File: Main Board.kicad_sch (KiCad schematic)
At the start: 114 parts, among them J102 Speaker Out, J110 SD Holder MEM2061-01-188-00-A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, J2 I2C_MAIN, J3 I2C_A, J4 I2C_B, J45 VCC Select, J49 NEOPIXEL AUX, J85 I2C_C, J86 I2C_D, J87 I2C_E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

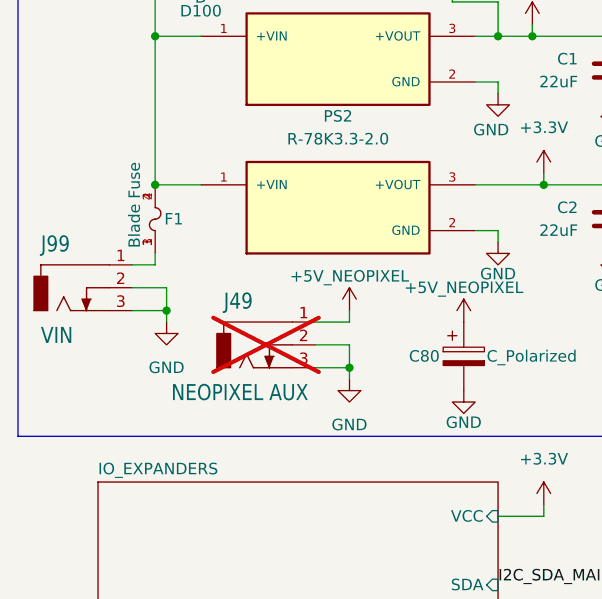
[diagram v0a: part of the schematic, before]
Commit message: Refining BOM & X4
X4 included a diode to protect from reverse polarity DC input. Begun work on Digikey BOM
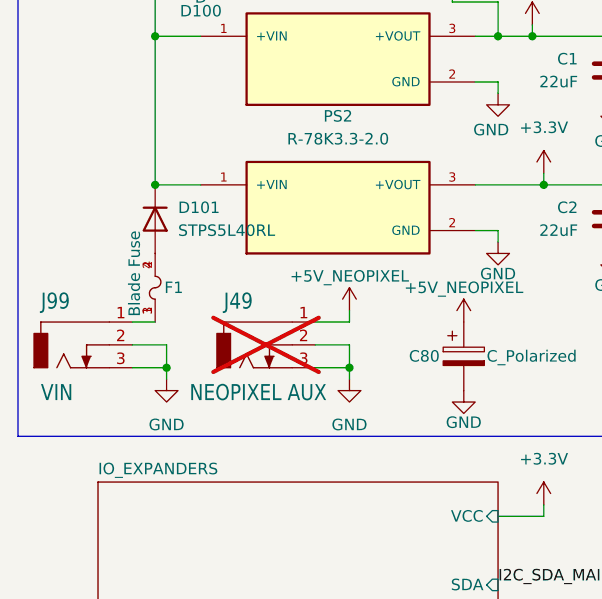
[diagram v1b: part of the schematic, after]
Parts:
- added D101: STPS5L40RL, Diode_THT:D_DO-201AD_P15.24mm_Horizontal, symbol Diode:1N5400
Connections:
- net +12V: now also D101.1 (K); no longer F1.2, F1.4
- new net: D101.2 (A), F1.2, F1.4
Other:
- moved on the sheet: F1, J99
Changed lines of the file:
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@@
 		(title "Main Universal Panel Board")
 		(date "2025-08-06")
-		(rev "X2")
+		(rev "X4")
 		(company "CMSC")
 		(comment 1 "NF 2025")
@@
 	)
 	(junction
-		(at 27.94 128.27)
-		(diameter 0)
-		(color 0 0 0 0)
-	)
-	(junction
 		(at 207.01 223.52)
 		(diameter 0)
@@
 	)
 	(junction
+		(at 27.94 128.27)
+		(diameter 0)
+		(color 0 0 0 0)
+	)
+	(junction
 		(at 358.14 77.47)
 		(diameter 0)
@@
 	)
 	(junction
-		(at 29.21 142.24)
+		(at 29.21 148.59)
 		(diameter 0)
 		(color 0 0 0 0)
@@
 	(wire
 		(pts
-			(xy 27.94 135.89) (xy 27.94 137.16)
-		)
-		(stroke
-			(width 0)
-			(type default)
-		)
-	)
-	(wire
-		(pts
 			(xy 39.37 57.15) (xy 39.37 59.69)
 		)
@@
 	(wire
 		(pts
-			(xy 29.21 142.24) (xy 29.21 143.51)
+			(xy 29.21 148.59) (xy 29.21 149.86)
 		)
 		(stroke
@@
 	(wire
 		(pts
-			(xy 27.94 137.16) (xy 25.4 137.16)
+			(xy 27.94 143.51) (xy 25.4 143.51)
 		)
 		(stroke
@@
 	(wire
 		(pts
-			(xy 29.21 139.7) (xy 29.21 142.24)
+			(xy 29.21 146.05) (xy 29.21 148.59)
 		)
 		(stroke
@@
 	(wire
 		(pts
-			(xy 25.4 139.7) (xy 29.21 139.7)
+			(xy 25.4 146.05) (xy 29.21 146.05)
 		)
 		(stroke
@@
 	(wire
 		(pts
-			(xy 25.4 142.24) (xy 29.21 142.24)
+			(xy 25.4 148.59) (xy 29.21 148.59)
 		)
 		(stroke
@@
 	)
 	(symbol
+		(lib_id "Diode:1N5400")
+		(at 27.94 132.08 270)
+		(unit 1)
+		(exclude_from_sim no)
+		(in_bom yes)
+		(on_board yes)
+		(dnp no)
+		(fields_autoplaced yes)
+		(property "Reference" "D101"
+			(at 30.48 130.8099 90)
+			(effects
+				(font
+					(size 1.27 1.27)
+				)
+				(justify left)
+			)
+		)
+		(property "Value" "STPS5L40RL"
+			(at 30.48 133.3499 90)
+			(effects
+				(font
+					(size 1.27 1.27)
+				)
+				(justify left)
+			)
+		)
+		(property "Footprint" "Diode_THT:D_DO-201AD_P15.24mm_Horizontal"
+			(at 23.495 132.08 0)
+			(effects
+				(font
+					(size 1.27 1.27)
+				)
+				(hide yes)
+			)
+		)
+		(property "Datasheet" "https://www.st.com/content/ccc/resource/technical/document/datasheet/18/17/66/c2/80/47/46/08/CD00002923.pdf/files/CD00002923.pdf/jcr:content/translations/en.CD00002923.pdf"
+			(at 27.94 132.08 0)
+			(effects
+				(font
+					(size 1.27 1.27)
+				)
+				(hide yes)
+			)
+		)
+		(property "Description" "Diode 40 V 5A Through Hole DO-201AD"
+			(at 27.94 132.08 0)
+			(effects
+				(font
+					(size 1.27 1.27)
+				)
+				(hide yes)
+			)
+		)
+		(property "Sim.Device" "D"
+			(at 27.94 132.08 0)
+			(effects
+				(font
+					(size 1.27 1.27)
+				)
+				(hide yes)
+			)
+		)
+		(property "Sim.Pins" "1=K 2=A"
+			(at 27.94 132.08 0)
+			(effects
+				(font
+					(size 1.27 1.27)
+				)
+				(hide yes)
+			)
+		)
+		(pin "2"
+		)
+		(pin "1"
+		)
+		(instances
+			(project ""
+				(path "/2aa9f2df-d06f-4a30-97ab-fb4628a40b5a"
+					(reference "D101")
+					(unit 1)
+				)
+			)
+		)
+	)
+	(symbol
 		(lib_id "power:+3.3V")
 		(at 120.65 144.78 0)
@@
 	(symbol
 		(lib_id "power:GND")
-		(at 29.21 143.51 0)
+		(at 29.21 149.86 0)
 		(mirror y)
 		(unit 1)
@@
 		(fields_autoplaced yes)
 		(property "Reference" "#PWR074"
-			(at 29.21 149.86 0)
+			(at 29.21 156.21 0)
 			(effects
 				(font
@@
 		)
 		(property "Value" "GND"
-			(at 29.21 148.59 0)
+			(at 29.21 154.94 0)
 			(effects
 				(font
@@
 		)
 		(property "Footprint" ""
-			(at 29.21 143.51 0)
+			(at 29.21 149.86 0)
 			(effects
 				(font
@@
 		)
 		(property "Datasheet" ""
-			(at 29.21 143.51 0)
+			(at 29.21 149.86 0)
 			(effects
 				(font
@@
 		)
 		(property "Description" "Power symbol creates a global label with name \"GND\" , ground"
-			(at 29.21 143.51 0)
+			(at 29.21 149.86 0)
 			(effects
 				(font
@@
 	(symbol
 		(lib_id "New_Panel_Parts:Blade Fuse Holder 3568")
-		(at 27.94 132.08 90)
+		(at 27.94 139.7 90)
 		(unit 1)
 		(exclude_from_sim no)
@@
 		(dnp no)
 		(property "Reference" "F1"
-			(at 28.956 132.08 90)
+			(at 28.956 139.7 90)
 			(effects
 				(font
@@
 		)
 		(property "Value" "Blade Fuse"
-			(at 25.654 125.73 0)
+			(at 25.654 133.35 0)
 			(effects
 				(font
@@
 		)
 		(property "Footprint" "New Panel Parts:FUSE_3568"
-			(at 18.034 131.826 0)
+			(at 18.034 139.446 0)
 			(effects
 				(font
@@
 		)
 		(property "Datasheet" ""
-			(at 27.94 132.08 0)
+			(at 27.94 139.7 0)
 			(effects
 				(font
@@
 		)
 		(property "Description" ""
-			(at 27.94 132.08 0)
+			(at 27.94 139.7 0)
 			(effects
 				(font
@@
 		)
 		(property "PARTREV" "C"
-			(at 18.034 131.826 0)
+			(at 18.034 139.446 0)
 			(effects
 				(font
@@
 		)
 		(property "MANUFACTURER" "Keystone"
-			(at 18.034 131.826 0)
+			(at 18.034 139.446 0)
 			(effects
 				(font
@@
 		)
 		(property "SNAPEDA_PN" "3568"
-			(at 18.034 131.826 0)
+			(at 18.034 139.446 0)
 			(effects
 				(font
@@
 		)
 		(property "MAXIMUM_PACKAGE_HEIGHT" "7.37 mm"
-			(at 18.034 131.826 0)
+			(at 18.034 139.446 0)
 			(effects
 				(font
@@
 		)
 		(property "STANDARD" "Manufacturer Recommendations"
-			(at 18.034 131.826 0)
+			(at 18.034 139.446 0)
 			(effects
 				(font
@@
 	(symbol
 		(lib_id "main-eagle-import:DCJ0303")
-		(at 17.78 139.7 0)
+		(at 17.78 146.05 0)
 		(unit 1)
 		(exclude_from_sim no)
@@
 		(dnp no)
 		(property "Reference" "J99"
-			(at 15.24 135.89 0)
+			(at 15.24 142.24 0)
 			(effects
 				(font
@@
 		)
 		(property "Value" "VIN"
-			(at 15.24 146.05 0)
+			(at 15.24 152.4 0)
 			(effects
 				(font
@@
 		)
 		(property "Footprint" "Connector_BarrelJack:BarrelJack_Horizontal"
-			(at 17.78 139.7 0)
+			(at 17.78 146.05 0)
 			(effects
 				(font
@@
 		)
 		(property "Datasheet" ""
-			(at 17.78 139.7 0)
+			(at 17.78 146.05 0)
 			(effects
 				(font
@@
 		)
 		(property "Description" ""
-			(at 17.78 139.7 0)
+			(at 17.78 146.05 0)
 			(effects
 				(font
@@
 		)
 		(property "Value" "NEOPIXEL AUX"
-			(at 29.718 152.4 0)
+			(at 31.75 152.4 0)
 			(effects
 				(font

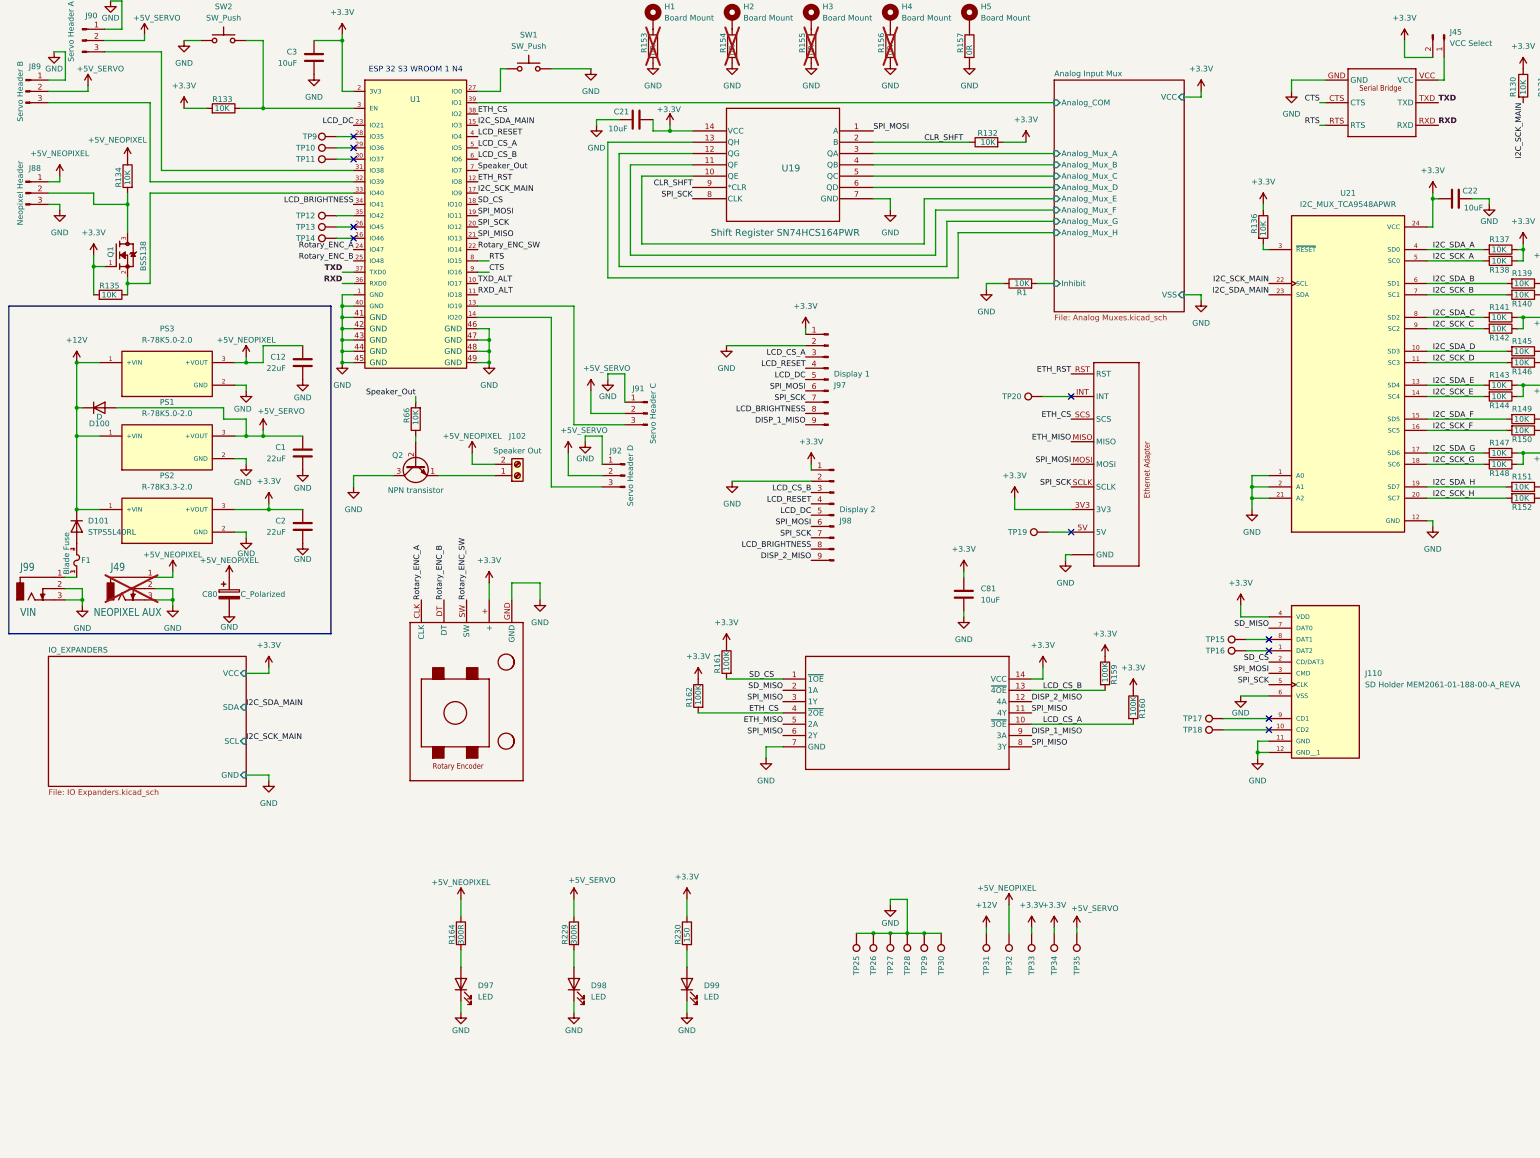
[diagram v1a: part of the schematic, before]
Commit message: Rev A0
REV A0 changes, additionally added STEP files for PAM8302, MAX98357, and JST XH 4 connector for UART. Updated KiCad schematic and PCB files, reorganized BOM and pick-and-place files for new revisions, and refreshed CAM data.
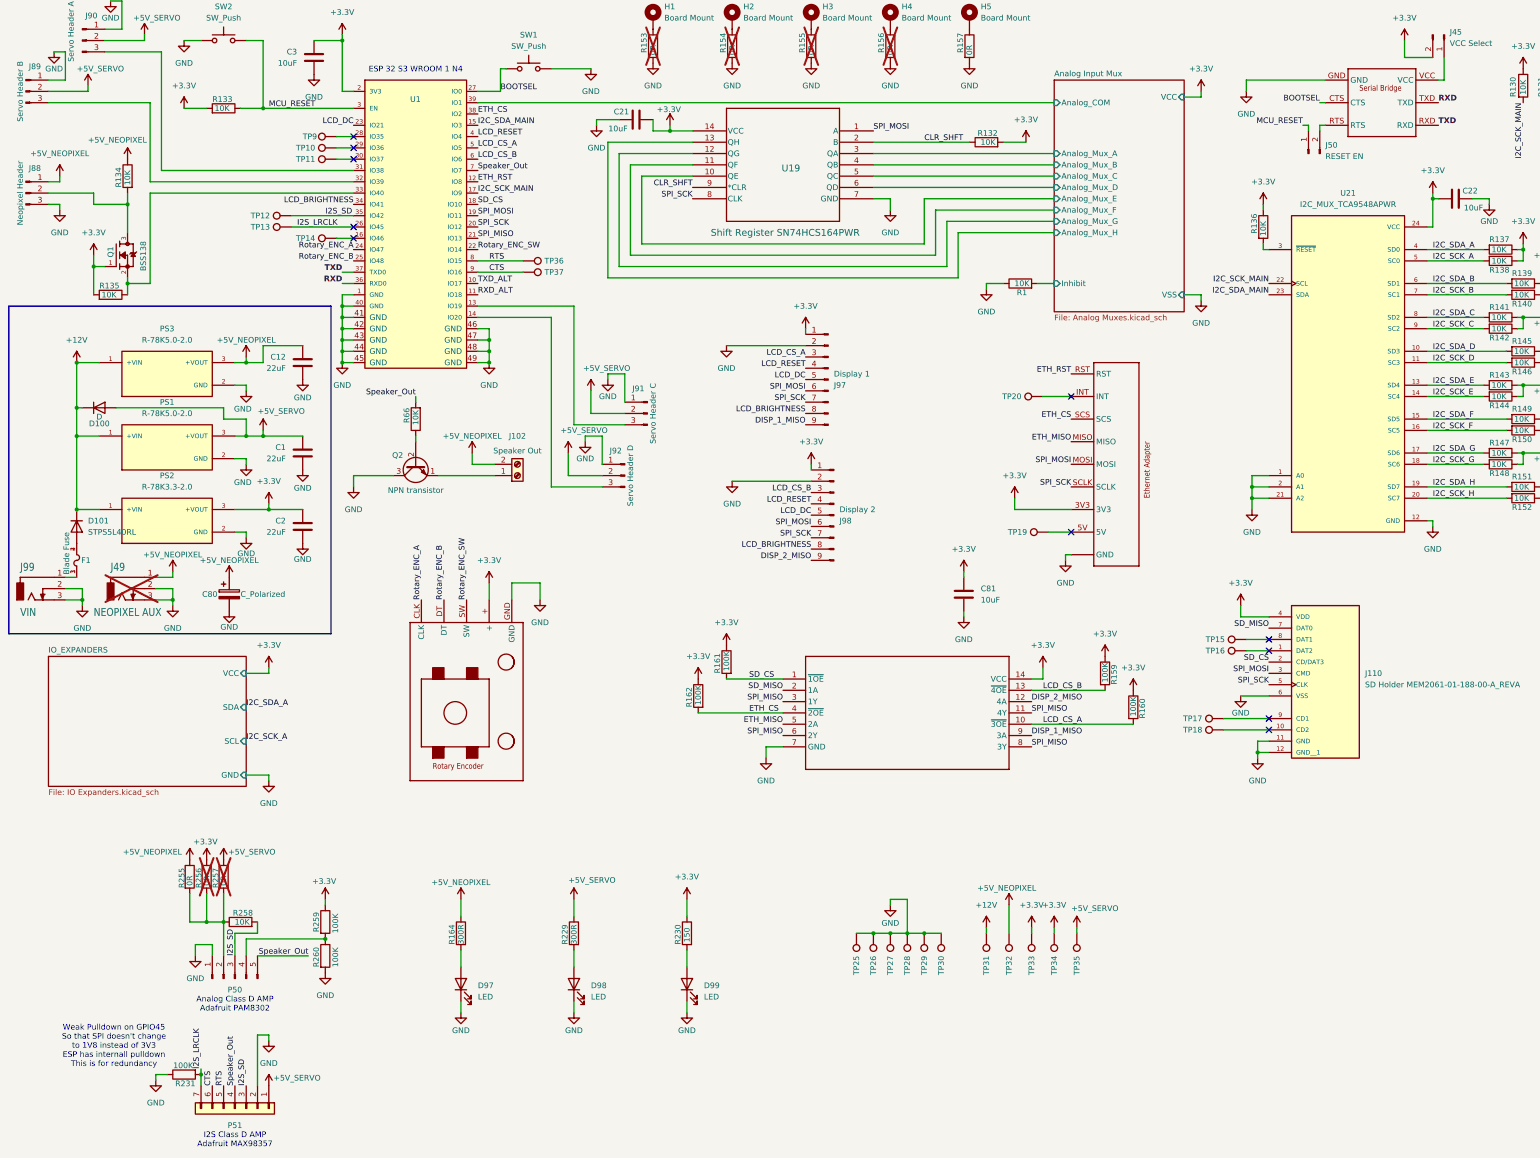
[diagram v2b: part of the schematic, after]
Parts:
- added J50: RESET EN, Connector_PinHeader_2.54mm:PinHeader_1x02_P2.54mm_Vertical, symbol Connector:Conn_01x02_Pin
- added P50: Conn_01x05_Pin, Connector_PinHeader_2.54mm:PinHeader_1x05_P2.54mm_Vertical, symbol Connector:Conn_01x05_Pin
- added P51: Conn_01x07, Connector_PinHeader_2.54mm:PinHeader_1x07_P2.54mm_Vertical, symbol Connector_Generic:Conn_01x07
- added R231, R259, R260: 100K, Resistor_SMD:R_0603_1608Metric, symbol Device:R
- added R255, R256, R257: 0R, Resistor_SMD:R_0603_1608Metric, symbol Device:R
- added R258: 10K, Resistor_SMD:R_0603_1608Metric, symbol Device:R
- added TP36, TP37: TestPoint, Connector_Pin:Pin_D1.0mm_L10.0mm, symbol Connector:TestPoint
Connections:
- net +3.3V: now also R256.1, R259.1
- net +5V_NEOPIXEL: now also R255.1
- net +5V_SERVO: now also P51.1 (Pin_1), R257.1
- net CTS: now also P51.6 (Pin_6), TP37.1; no longer J1.CTS
- net GND: now also P50.1 (Pin_1), P51.2 (Pin_2), R231.1, R260.2
- net RTS: now also P51.5 (Pin_5), TP36.1; no longer J1.RTS
- net RXD: now also J1.TXD; no longer J1.RXD
- net Speaker_Out: now also P50.5 (Pin_5), P51.4 (Pin_4)
- net TXD: now also J1.RXD; no longer J1.TXD
- net MCU_RESET: now reaches R133.1, SW2.1, U1.3 (EN)
- net MCU_RESET: now also J50.1 (Pin_1)
- net I2S_LRCLK: now reaches TP13.1, U1.26 (IO45)
- net I2S_LRCLK: now also P51.7 (Pin_7), R231.2
- net BOOTSEL: now reaches SW1.1, U1.27 (IO0)
- net BOOTSEL: now also J1.CTS
- net I2S_SD: now reaches TP12.1, U1.35 (IO42)
- net I2S_SD: now also P50.3 (Pin_3), P51.3 (Pin_3), R258.2
- new net: P50.2 (Pin_2), R255.2, R256.2, R257.2, R258.1
- new net: P50.4 (Pin_4), R259.2, R260.1
- new net: J1.RTS, J50.2 (Pin_2)
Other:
- note added: "Analog Class D AMP Adafruit PAM8302"
- note added: "I2S Class D AMP Adafruit MAX98357"
- note added: "Weak Pulldown on GPIO45 So that SPI doesn't change to 1V8 instead of 3V3 ESP has internall pulldown This is for redundancy"
- moved on the sheet: TP12, TP13

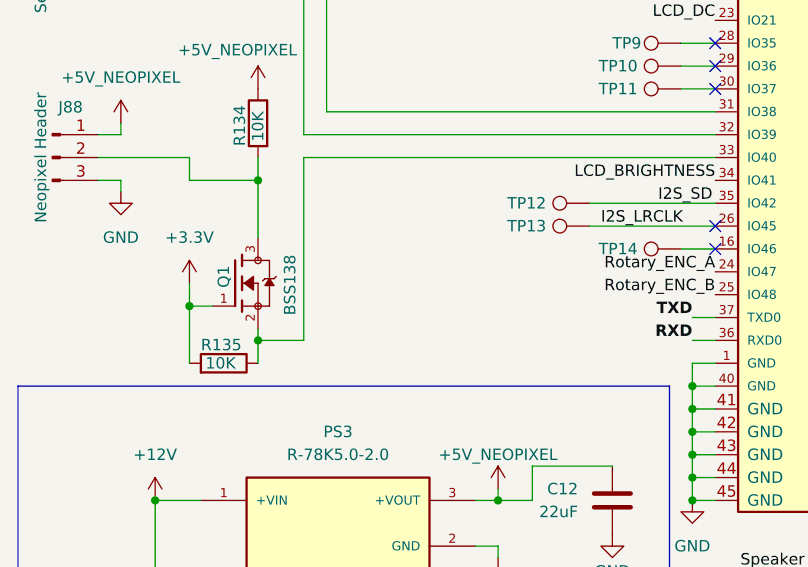
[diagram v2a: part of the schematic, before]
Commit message: Added 2 test points
for possible logic level converters
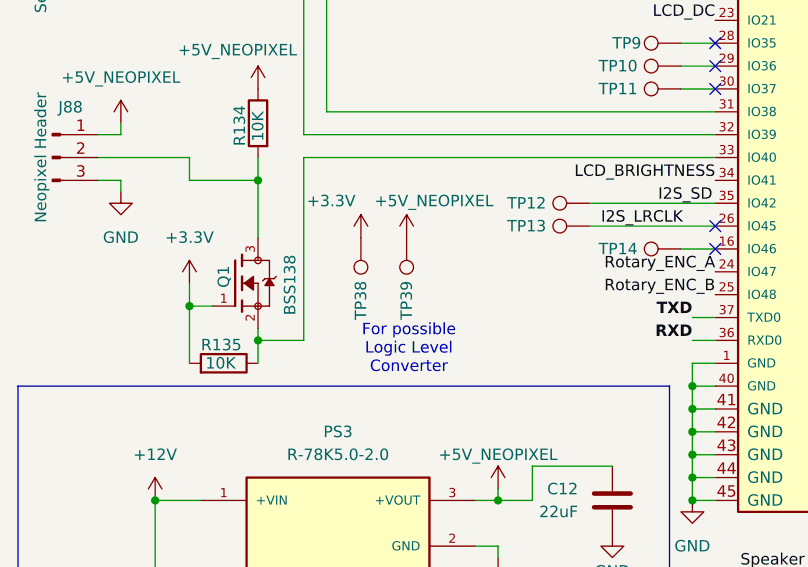
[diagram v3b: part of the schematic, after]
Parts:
- added TP38, TP39: TestPoint, Connector_Pin:Pin_D1.0mm_L10.0mm, symbol Connector:TestPoint
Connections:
- net +3.3V: now also TP38.1
- net +5V_NEOPIXEL: now also TP39.1
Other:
- note added: "For possible Logic Level Converter"
